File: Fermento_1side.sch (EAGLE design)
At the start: 25 parts, among them Q1 32.768kHz, Q2 P-MOSFET

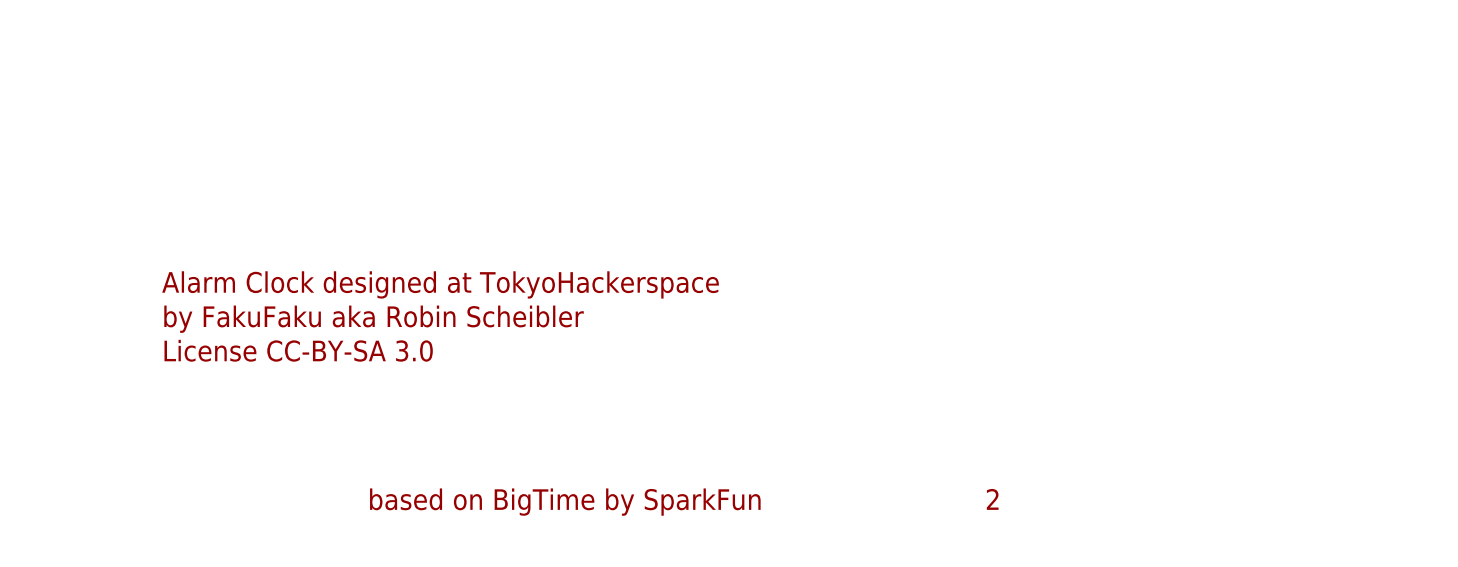
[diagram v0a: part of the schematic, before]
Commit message: Added 1 sided version and png images.
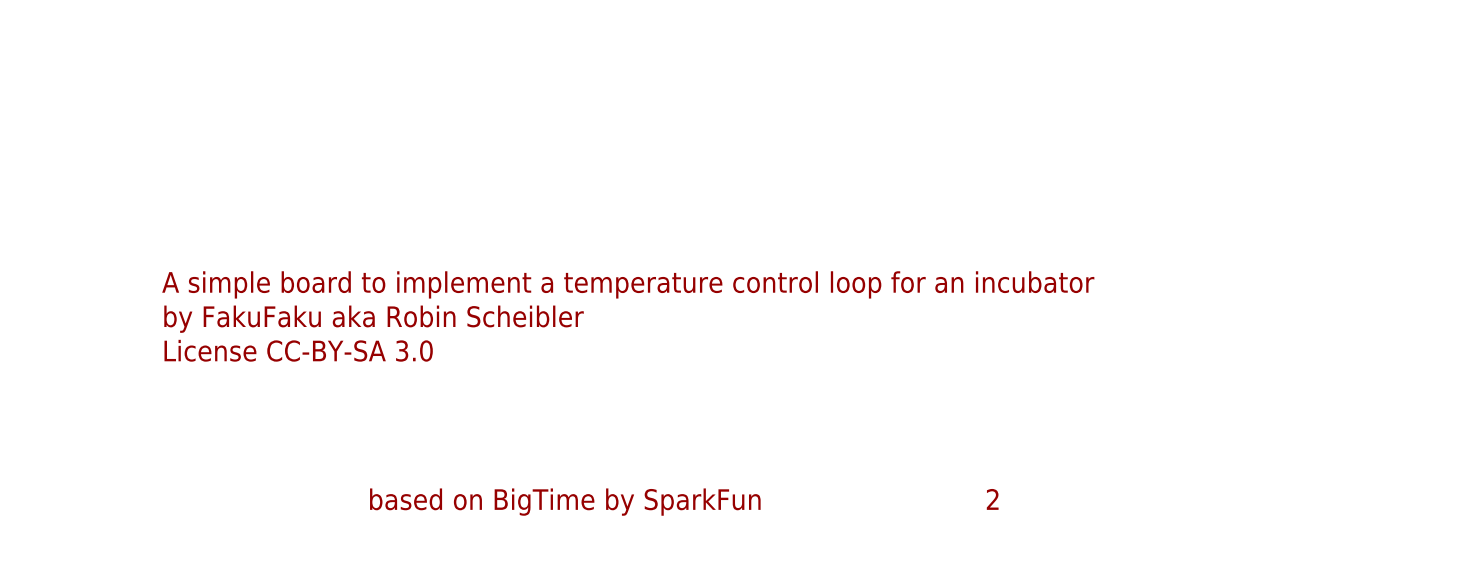
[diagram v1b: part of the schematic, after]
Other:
- note added: "A simple board to implement a temperature control loop for an incubator"
- note removed: "Alarm Clock designed at TokyoHackerspace"
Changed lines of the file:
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@@
 <sheet>
 <plain>
-<text x="167.64" y="-173.99" size="2.286" layer="94">Alarm Clock designed at TokyoHackerspace</text>
+<text x="167.64" y="-173.99" size="2.286" layer="94">A simple board to implement a temperature control loop for an incubator</text>
 <text x="167.64" y="-177.8" size="2.286" layer="94">by FakuFaku aka Robin Scheibler</text>
 <text x="167.64" y="-181.61" size="2.286" layer="94">License CC-BY-SA 3.0</text>

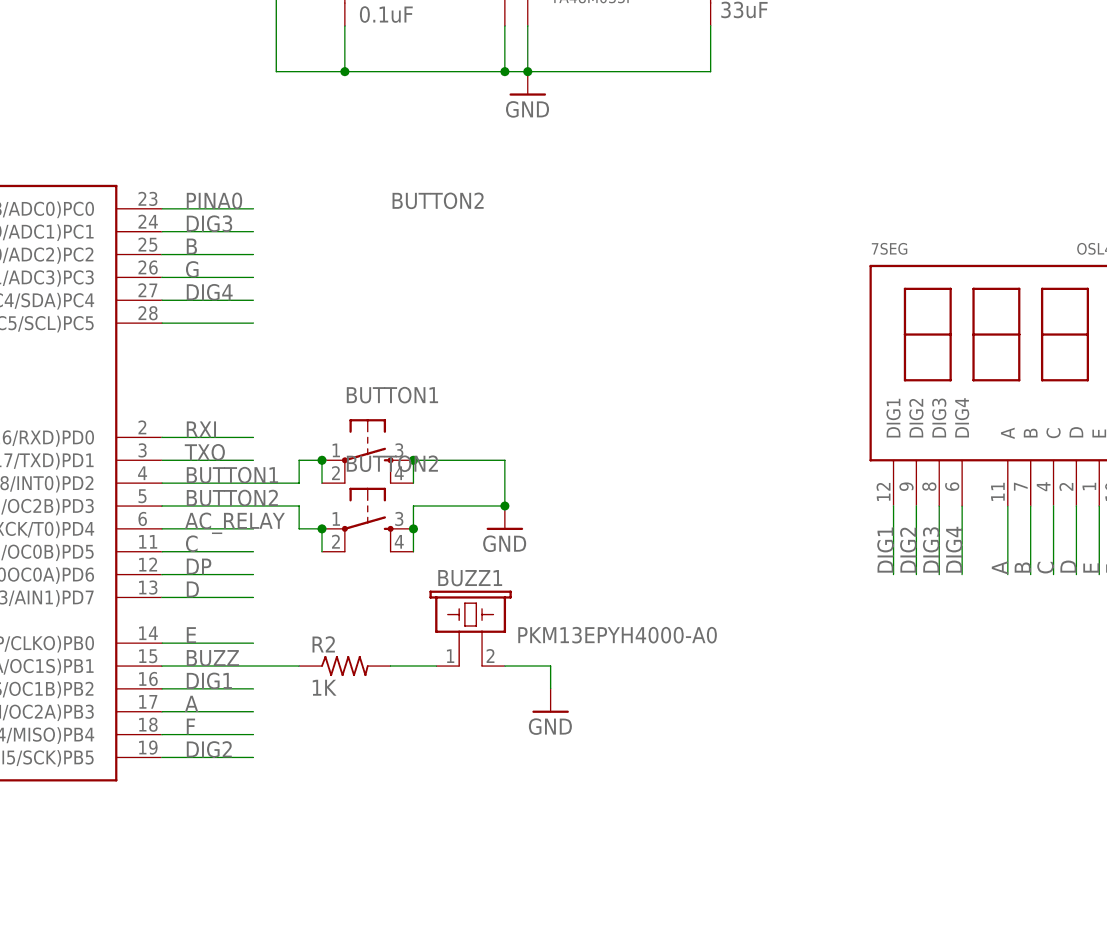
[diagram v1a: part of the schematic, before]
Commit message: Added mask and info diagram for 1sided homebrew incubator.
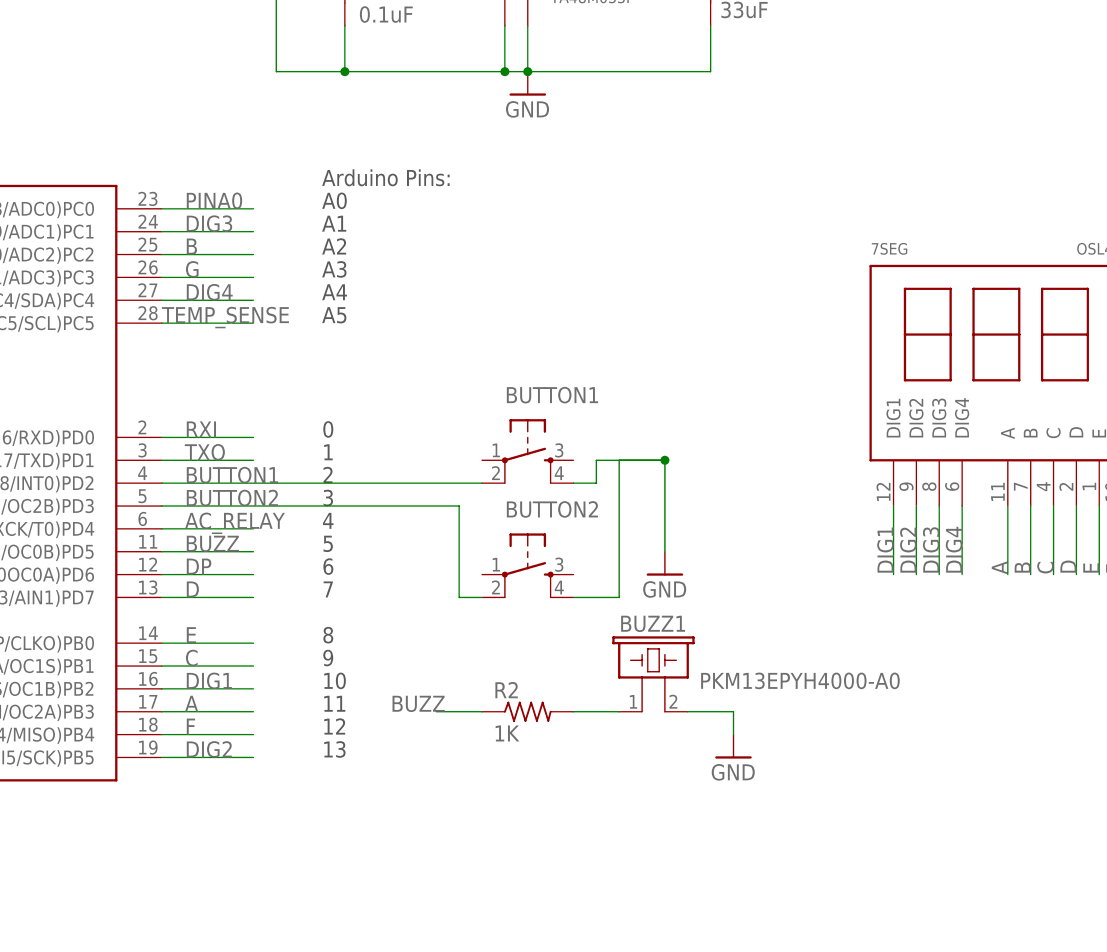
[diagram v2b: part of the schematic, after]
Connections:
- net BUTTON1: no longer BUTTON1.1
- net BUTTON2: no longer BUTTON2.1
- net BUZZ: now also ATMEGA328.(PCI21/T1/OC0B)PD5; no longer ATMEGA328.(PCI1/OC1A/OC1S)PB1
- net C: now also ATMEGA328.(PCI1/OC1A/OC1S)PB1; no longer ATMEGA328.(PCI21/T1/OC0B)PD5
- net GND: no longer BUTTON1.3, BUTTON2.3
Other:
- note added: "0"
- note added: "1"
- note added: "10"
- note added: "11"
- note added: "12"
- note added: "13"
- note added: "3"
- note added: "4"
- note added: "5"
- note added: "6"
- note added: "7"
- note added: "8"
- note added: "9"
- note added: "A0"
- note added: "A1"
- note added: "A2"
- note added: "A3"
- note added: "A4"
- note added: "A5"
- note added: "Arduino Pins:"
- moved on the sheet: BUTTON1, BUTTON2, BUZZ1, R2
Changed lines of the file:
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@@
 <text x="259.08" y="-198.12" size="2.286" layer="94">2</text>
 <text x="190.5" y="-198.12" size="2.286" layer="94">based on BigTime by SparkFun</text>
+<text x="132.08" y="-81.28" size="1.778" layer="97">0</text>
+<text x="132.08" y="-83.82" size="1.778" layer="97">1</text>
+<text x="132.08" y="-86.36" size="1.778" layer="97">2</text>
+<text x="132.08" y="-88.9" size="1.778" layer="97">3</text>
+<text x="132.08" y="-91.44" size="1.778" layer="97">4</text>
+<text x="132.08" y="-93.98" size="1.778" layer="97">5</text>
+<text x="132.08" y="-96.52" size="1.778" layer="97">6</text>
+<text x="132.08" y="-99.06" size="1.778" layer="97">7</text>
+<text x="132.08" y="-104.14" size="1.778" layer="97">8</text>
+<text x="132.08" y="-106.68" size="1.778" layer="97">9</text>
+<text x="132.08" y="-109.22" size="1.778" layer="97">10</text>
+<text x="132.08" y="-111.76" size="1.778" layer="97">11</text>
+<text x="132.08" y="-114.3" size="1.778" layer="97">12</text>
+<text x="132.08" y="-116.84" size="1.778" layer="97">13</text>
+<text x="132.08" y="-55.88" size="1.778" layer="97">A0</text>
+<text x="132.08" y="-58.42" size="1.778" layer="97">A1</text>
+<text x="132.08" y="-60.96" size="1.778" layer="97">A2</text>
+<text x="132.08" y="-63.5" size="1.778" layer="97">A3</text>
+<text x="132.08" y="-66.04" size="1.778" layer="97">A4</text>
+<text x="132.08" y="-68.58" size="1.778" layer="97">A5</text>
+<text x="132.08" y="-53.34" size="1.778" layer="97">Arduino Pins:</text>
 </plain>
 <instances>
@@
 <instance part="C2" gate="G$1" x="40.64" y="-99.06"/>
 <instance part="R1" gate="G$1" x="58.42" y="-43.18" rot="R90"/>
-<instance part="R2" gate="G$1" x="134.62" y="-106.68"/>
-<instance part="BUTTON1" gate="S" x="137.16" y="-83.82"/>
+<instance part="R2" gate="G$1" x="154.94" y="-111.76"/>
+<instance part="BUTTON1" gate="S" x="154.94" y="-83.82"/>
 <instance part="C3" gate="G$1" x="81.28" y="-38.1" rot="R270"/>
 <instance part="GND1" gate="1" x="40.64" y="-78.74"/>
 <instance part="GND2" gate="1" x="40.64" y="-109.22"/>
 <instance part="Q1" gate="G$1" x="53.34" y="-76.2" rot="R90"/>
-<instance part="BUZZ1" gate="G$1" x="147.32" y="-104.14"/>
+<instance part="BUZZ1" gate="G$1" x="167.64" y="-109.22"/>
 <instance part="TEMP1" gate="G$1" x="231.14" y="-25.4"/>
 <instance part="P+2" gate="1" x="40.64" y="-88.9"/>
-<instance part="GND3" gate="1" x="152.4" y="-91.44"/>
-<instance part="GND4" gate="1" x="157.48" y="-111.76"/>
+<instance part="GND3" gate="1" x="170.18" y="-96.52"/>
+<instance part="GND4" gate="1" x="177.8" y="-116.84"/>
 <instance part="P+3" gate="1" x="58.42" y="-27.94"/>
 <instance part="GND5" gate="1" x="231.14" y="-40.64"/>
@@
 <instance part="H4" gate="G$1" x="33.02" y="-205.74"/>
 <instance part="SERIAL" gate="A" x="93.98" y="-33.02"/>
-<instance part="BUTTON2" gate="S" x="137.16" y="-91.44"/>
+<instance part="BUTTON2" gate="S" x="154.94" y="-96.52"/>
 <instance part="Q2" gate="G$1" x="53.34" y="-162.56"/>
 <instance part="P+1" gate="1" x="55.88" y="-149.86"/>
@@
 </segment>
 <segment>
-<wire x1="142.24" y1="-83.82" x2="152.4" y2="-83.82" width="0.1524" layer="91"/>
-<wire x1="152.4" y1="-83.82" x2="152.4" y2="-88.9" width="0.1524" layer="91"/>
-<pinref part="BUTTON1" gate="S" pin="3"/>
+<wire x1="170.18" y1="-83.82" x2="170.18" y2="-93.98" width="0.1524" layer="91"/>
 <pinref part="GND3" gate="1" pin="GND"/>
-<junction x="152.4" y="-88.9"/>
-<pinref part="BUTTON2" gate="S" pin="3"/>
-<wire x1="142.24" y1="-91.44" x2="142.24" y2="-88.9" width="0.1524" layer="91"/>
-<wire x1="142.24" y1="-88.9" x2="152.4" y2="-88.9" width="0.1524" layer="91"/>
-<junction x="142.24" y="-91.44"/>
-<junction x="142.24" y="-83.82"/>
+<junction x="170.18" y="-83.82"/>
 <pinref part="BUTTON2" gate="S" pin="4"/>
-<wire x1="142.24" y1="-91.44" x2="142.24" y2="-93.98" width="0.1524" layer="91"/>
+<wire x1="160.02" y1="-99.06" x2="165.1" y2="-99.06" width="0.1524" layer="91"/>
+<wire x1="165.1" y1="-99.06" x2="165.1" y2="-83.82" width="0.1524" layer="91"/>
+<wire x1="165.1" y1="-83.82" x2="170.18" y2="-83.82" width="0.1524" layer="91"/>
 <pinref part="BUTTON1" gate="S" pin="4"/>
-<wire x1="142.24" y1="-83.82" x2="142.24" y2="-86.36" width="0.1524" layer="91"/>
-</segment>
-<segment>
-<wire x1="152.4" y1="-106.68" x2="157.48" y2="-106.68" width="0.1524" layer="91"/>
-<wire x1="157.48" y1="-106.68" x2="157.48" y2="-109.22" width="0.1524" layer="91"/>
+<wire x1="160.02" y1="-86.36" x2="162.56" y2="-86.36" width="0.1524" layer="91"/>
+<wire x1="162.56" y1="-86.36" x2="162.56" y2="-83.82" width="0.1524" layer="91"/>
+<wire x1="162.56" y1="-83.82" x2="170.18" y2="-83.82" width="0.1524" layer="91"/>
+</segment>
+<segment>
+<wire x1="172.72" y1="-111.76" x2="177.8" y2="-111.76" width="0.1524" layer="91"/>
+<wire x1="177.8" y1="-111.76" x2="177.8" y2="-114.3" width="0.1524" layer="91"/>
 <pinref part="BUZZ1" gate="G$1" pin="2"/>
 <pinref part="GND4" gate="1" pin="GND"/>
@@
 </segment>
 </net>
-<net name="BUZZ" class="0">
-<segment>
-<wire x1="114.3" y1="-106.68" x2="129.54" y2="-106.68" width="0.1524" layer="91"/>
-<label x="116.84" y="-106.68" size="1.778" layer="95"/>
-<pinref part="ATMEGA328" gate="G$1" pin="(PCI1/OC1A/OC1S)PB1"/>
-<pinref part="R2" gate="G$1" pin="1"/>
-</segment>
-</net>
 <net name="N$13" class="0">
 <segment>
-<wire x1="139.7" y1="-106.68" x2="144.78" y2="-106.68" width="0.1524" layer="91"/>
+<wire x1="160.02" y1="-111.76" x2="165.1" y2="-111.76" width="0.1524" layer="91"/>
 <pinref part="R2" gate="G$1" pin="2"/>
 <pinref part="BUZZ1" gate="G$1" pin="1"/>
@@
 <pinref part="ATMEGA328" gate="G$1" pin="(PCI13/ADC5/SCL)PC5"/>
 <wire x1="114.3" y1="-68.58" x2="124.46" y2="-68.58" width="0.1524" layer="91"/>
+<label x="114.3" y="-68.58" size="1.778" layer="95"/>
 </segment>
 </net>
@@
 </segment>
 <segment>
+<pinref part="ATMEGA328" gate="G$1" pin="(PCI3/MOSI/OC2A)PB3"/>
 <wire x1="114.3" y1="-111.76" x2="124.46" y2="-111.76" width="0.1524" layer="91"/>
 <label x="116.84" y="-111.76" size="1.778" layer="95"/>
-<pinref part="ATMEGA328" gate="G$1" pin="(PCI3/MOSI/OC2A)PB3"/>
 </segment>
 </net>
@@
 </segment>
 <segment>
-<wire x1="114.3" y1="-93.98" x2="124.46" y2="-93.98" width="0.1524" layer="91"/>
-<label x="116.84" y="-93.98" size="1.778" layer="95"/>
-<pinref part="ATMEGA328" gate="G$1" pin="(PCI21/T1/OC0B)PD5"/>
+<pinref part="ATMEGA328" gate="G$1" pin="(PCI1/OC1A/OC1S)PB1"/>
+<wire x1="114.3" y1="-106.68" x2="124.46" y2="-106.68" width="0.1524" layer="91"/>
+<label x="116.84" y="-106.68" size="1.778" layer="95"/>
 </segment>
 </net>
@@
 <net name="BUTTON1" class="0">
 <segment>
-<wire x1="114.3" y1="-86.36" x2="129.54" y2="-86.36" width="0.1524" layer="91"/>
-<wire x1="129.54" y1="-86.36" x2="129.54" y2="-83.82" width="0.1524" layer="91"/>
-<wire x1="129.54" y1="-83.82" x2="132.08" y2="-83.82" width="0.1524" layer="91"/>
+<wire x1="114.3" y1="-86.36" x2="149.86" y2="-86.36" width="0.1524" layer="91"/>
 <label x="116.84" y="-86.36" size="1.778" layer="95"/>
 <pinref part="ATMEGA328" gate="G$1" pin="(PCI18/INT0)PD2"/>
-<pinref part="BUTTON1" gate="S" pin="1"/>
-<junction x="132.08" y="-83.82"/>
 <pinref part="BUTTON1" gate="S" pin="2"/>
-<wire x1="132.08" y1="-83.82" x2="132.08" y2="-86.36" width="0.1524" layer="91"/>
 </segment>
 </net>
 <net name="BUTTON2" class="0">
 <segment>
-<wire x1="114.3" y1="-88.9" x2="129.54" y2="-88.9" width="0.1524" layer="91"/>
+<wire x1="114.3" y1="-88.9" x2="147.32" y2="-88.9" width="0.1524" layer="91"/>
 <label x="116.84" y="-88.9" size="1.778" layer="95"/>
 <pinref part="ATMEGA328" gate="G$1" pin="(PCI19/INT1/OC2B)PD3"/>
-<wire x1="129.54" y1="-88.9" x2="129.54" y2="-91.44" width="0.1524" layer="91"/>
-<label x="139.7" y="-55.88" size="1.778" layer="95"/>
-<pinref part="BUTTON2" gate="S" pin="1"/>
 <pinref part="BUTTON2" gate="S" pin="2"/>
-<wire x1="132.08" y1="-91.44" x2="132.08" y2="-93.98" width="0.1524" layer="91"/>
-<junction x="132.08" y="-91.44"/>
-<wire x1="129.54" y1="-91.44" x2="132.08" y2="-91.44" width="0.1524" layer="91"/>
+<wire x1="147.32" y1="-88.9" x2="147.32" y2="-99.06" width="0.1524" layer="91"/>
+<wire x1="147.32" y1="-99.06" x2="149.86" y2="-99.06" width="0.1524" layer="91"/>
 </segment>
 </net>
@@
 </segment>
 </net>
+<net name="BUZZ" class="0">
+<segment>
+<wire x1="114.3" y1="-93.98" x2="124.46" y2="-93.98" width="0.1524" layer="91"/>
+<label x="116.84" y="-93.98" size="1.778" layer="95"/>
+<pinref part="ATMEGA328" gate="G$1" pin="(PCI21/T1/OC0B)PD5"/>
+</segment>
+<segment>
+<pinref part="R2" gate="G$1" pin="1"/>
+<wire x1="149.86" y1="-111.76" x2="144.78" y2="-111.76" width="0.1524" layer="91"/>
+<label x="139.7" y="-111.76" size="1.778" layer="95"/>
+</segment>
+</net>
